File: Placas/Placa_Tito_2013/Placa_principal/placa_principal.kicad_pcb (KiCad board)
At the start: 2 copper layers, 65 x 100 mm, 83 parts, among them IC1 ATMEGA88-P, K1 Servo, K2 Jumper con doble posicion, P1 Puerto Serie, P10 CONN_1, P11 CONN_1, P12 CONN_1, P13 CONN_1, P14 CONN_1, P15 CONN_1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

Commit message: Mejoras a placa principal
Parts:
- removed the 1PIN at (59.5, 65.0)
- removed the 1PIN2mm at (59.5, 65.0)
- removed R1, R2: R sensor, R3
- removed R8, R9: 100, R1
- removed RV5, RV6: POT, PIN_ARRAY_3X1
- removed SERVO_U1, SERVO_U2: CNY70, cny70-4
- added 1PIN: P***, 1pin, F.Cu at (49.5, 63.2)
- added 1PIN: P***, 1pin, F.Cu at (77.5, 63.2)
- added 1PIN: P***, 1pin, F.Cu at (59.5, 63.2)
- U3, U4, U6, U7: moved to B.Cu
- moved RV3 9.46 mm to (85.7, 57.2), turned to 180 degrees
- moved R11 5.09 mm to (82.5, 63.9)
- moved C7 3.96 mm to (42.3, 62.6)
- moved R12 3.58 mm to (45.0, 63.8)
- moved R5 3.08 mm to (30.3, 66.1)
- moved RV2 2.61 mm to (33.1, 64.5)
- moved R6 1.90 mm to (86.4, 64.0)
- moved R7 1.64 mm to (78.2, 78.3)
- moved R10 1.26 mm to (39.8, 66.9)
- moved K2 0.81 mm to (78.7, 127.1)
- moved JP2 0.60 mm to (62.0, 132.0)
- moved P5 0.36 mm to (87.8, 127.2)
- turned U3 to 180 degrees
- turned U4 to 180 degrees
- turned U6 to 180 degrees
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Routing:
- net GND: track 570.2 -> 505.0 mm, vias 6 -> 10
- net /IN_1A: track 149.1 -> 124.3 mm
- net /SENSOR 3: track 134.5 -> 152.9 mm
- net N-000007: track 49.7 -> 38.9 mm, vias 0 -> 1
- net N-0000051: track 9.08 -> 16.5 mm
- net /SCK: track 42.1 -> 36.0 mm
- net /LED3: track 37.9 -> 43.7 mm
- net +8V: track 126.6 -> 132.3 mm, vias 3 -> 2
- net /SENSOR 4: track 88.1 -> 92.5 mm, vias 2 -> 3
- net N-000008: track 6.40 -> 10.6 mm, vias 0 -> 1
- net N-0000050: track 16.3 -> 12.3 mm
- net N-0000054: track 61.5 -> 58.6 mm
- net /IN_2A: track 108.9 -> 106.2 mm
- net /IN_4B: track 30.6 -> 33.3 mm
- net N-0000034: track 5.32 -> 3.02 mm
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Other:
- board size 65 x 100 mm -> 65 x 103.4 mm
- net class Default: via_dia 0.889 -> 1.397

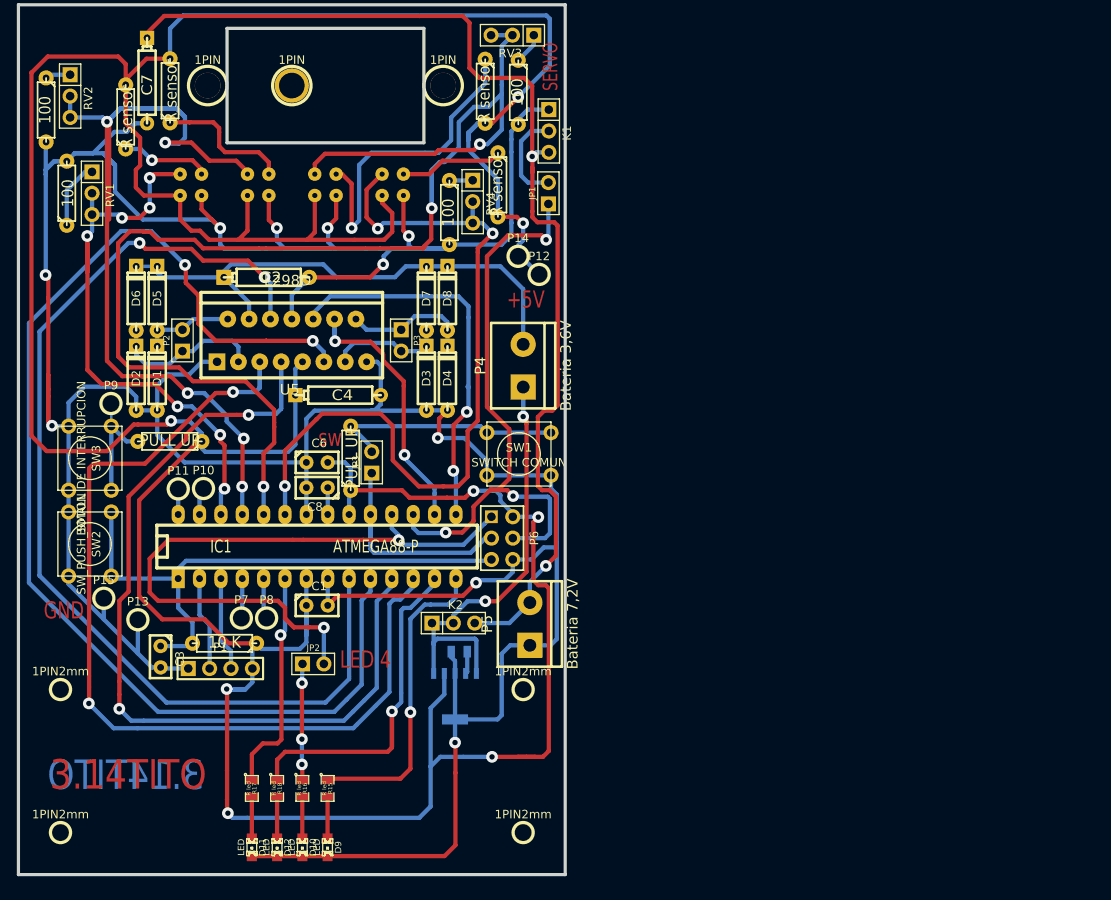
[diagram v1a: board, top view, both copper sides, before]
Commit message: Se termino de routear la placa con los nuevos sensores
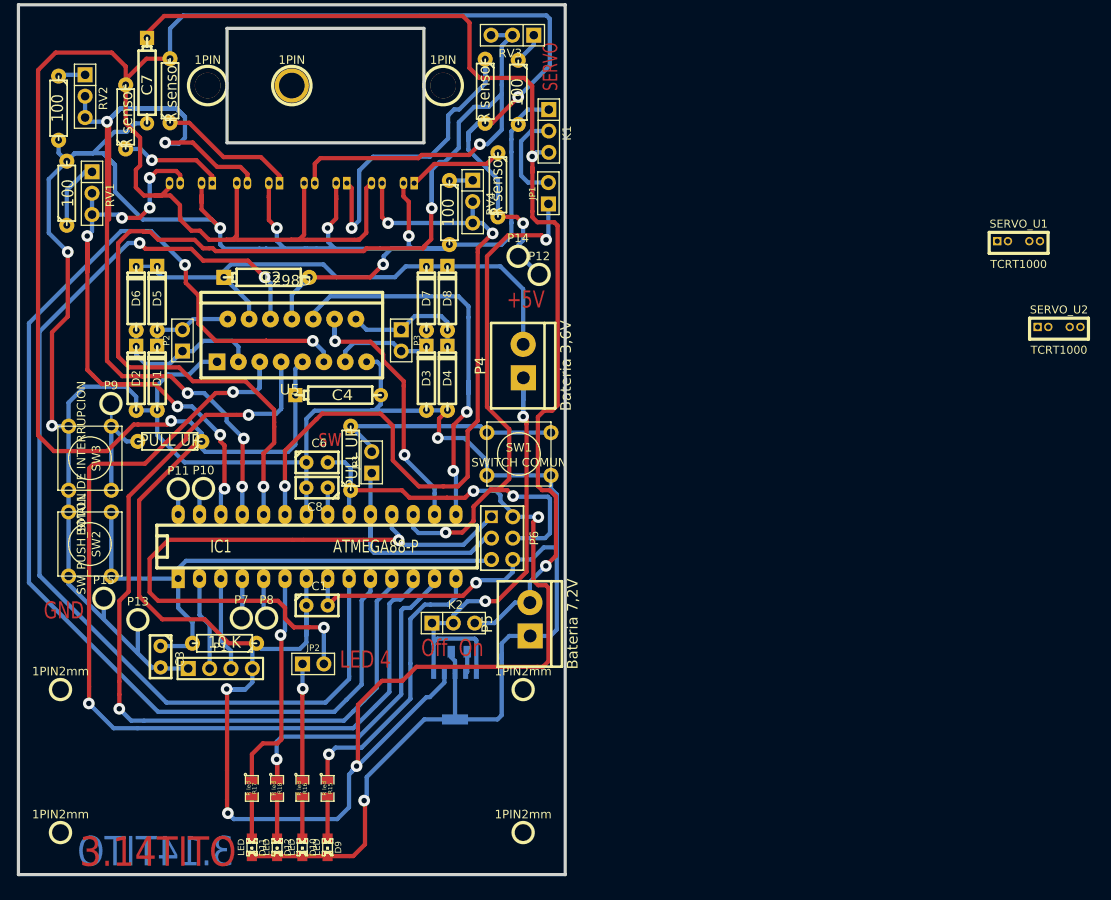
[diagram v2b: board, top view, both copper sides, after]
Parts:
- added SERVO_U1: TCRT1000, TCRT1000, F.Cu at (145.9, 81.9)
- added SERVO_U2: TCRT1000, TCRT1000, F.Cu at (150.7, 92.1)
- U3, U4, U6, U7: value CNY70 -> TCRT1000; footprint cny70-4 -> TCRT1000
- moved RV2 1.78 mm to (34.9, 64.5)
- moved R5 1.50 mm to (31.8, 65.9)
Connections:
- R10 pad 1: N-000008 -> N-0000039
- R11 pad 1: N-000007 -> N-0000037
- R12 pad 1: N-0000051 -> N-0000029
- R13 pad 1: N-0000050 -> N-0000025
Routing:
- net N-0000037: track 0.00 -> 39.4 mm, vias 0 -> 1
- net N-000007: track 38.9 -> 0.00 mm, vias 1 -> 0
- net N-0000029: track 0.00 -> 16.6 mm
- net N-0000051: track 16.5 -> 0.00 mm
- net +5V: track 481.1 -> 494.1 mm
- net N-0000039: track 0.00 -> 12.5 mm, vias 0 -> 1
- net N-0000050: track 12.3 -> 0.00 mm
- net N-0000025: track 0.00 -> 11.5 mm
- net N-000008: track 10.6 -> 0.00 mm, vias 1 -> 0
- net GND: track 505.0 -> 498.3 mm
- net /SENSOR 4: track 92.5 -> 88.3 mm
- net /LED3: track 43.7 -> 40.1 mm
- net /LED1: track 36.9 -> 33.8 mm
- net N-0000040: track 58.6 -> 61.2 mm
- net /SENSOR 3: track 152.9 -> 154.3 mm
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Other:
- board text added: "Off On"

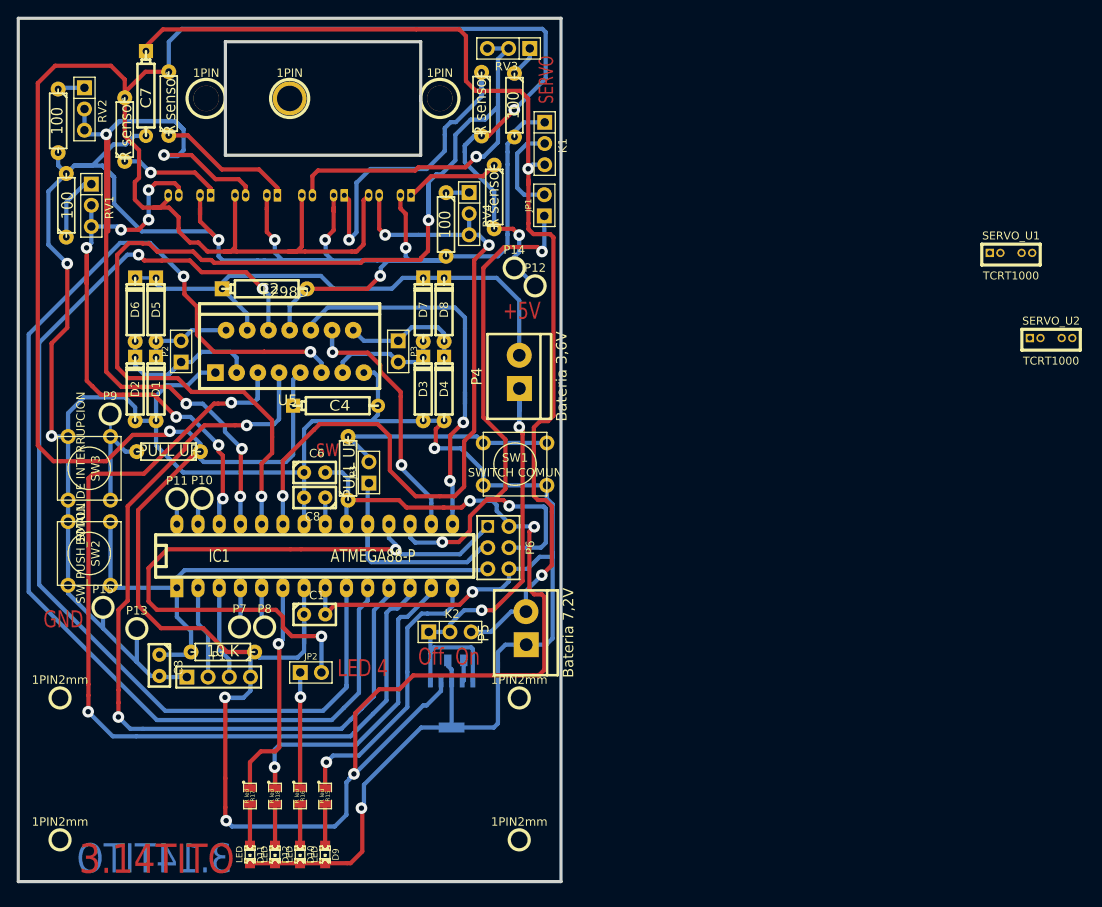
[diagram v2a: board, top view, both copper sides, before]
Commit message: Asociado componente que faltaba, reseteados componentes de la placa.
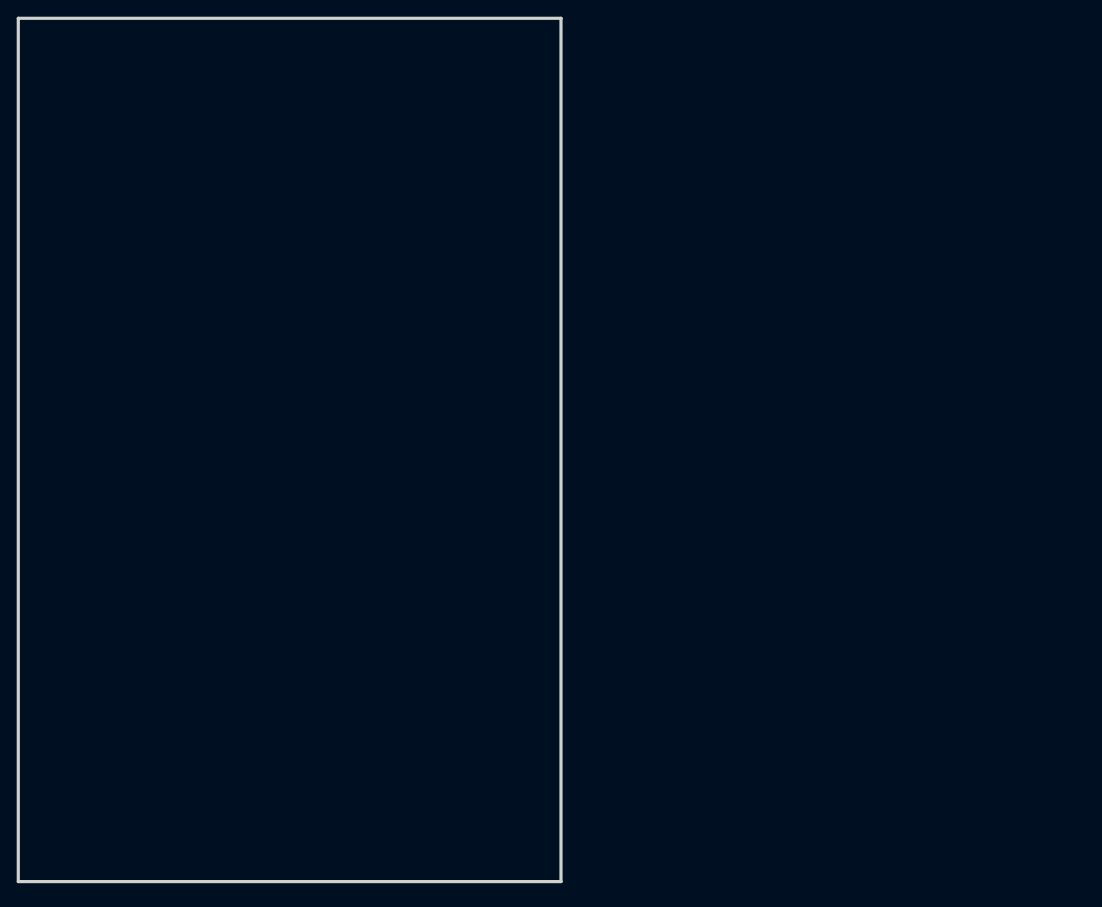
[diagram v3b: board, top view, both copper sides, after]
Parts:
- removed 1PIN (x3): P***, 1pin
- removed 1PIN2mm (x4): P***, 1PIN2mm
- removed C1: 100 nF, C1
- removed C2: 1000 uF, CP4
- removed C3: 100n, C1
- removed C4: 220 uF, CP4
- removed C5: 10 nF, SM0805
- removed C6, C8: 100nF, C1
- removed C7: 100uF, CP4
- removed D1, D2, D3, D4, D5, D6, D7, D8: DIODE, D3
- removed D10, D11, D12, D9: LED, LED-0805
- removed IC1: ATMEGA88-P, DIP-28__300_ELL
- removed JP1, JP2, JP3: JUMPER, PIN_ARRAY_2X1
- removed K1: Servo, PIN_ARRAY_3X1
- removed K2: Jumper con doble posicion, PIN_ARRAY_3X1
- removed P1: Puerto Serie, PIN_ARRAY_4x1
- removed P10, P11, P12, P13, P14, P15, P7, P8, P9: CONN_1, 1PIN2mm
- removed P2: Motor 1, PIN_ARRAY_2X1
- removed P3: Motor 2, PIN_ARRAY_2X1
- removed P4: Bateria 3,6V, bornier2
- removed P5: Bateria 7,2V, bornier2
- removed P6: Programador, pin_array_3x2
- removed R10, R11, R12, R13: R sensor, R3
- removed R14: 10 K, R3
- removed R15, R16, R17, R18: R led, SM0805
- removed R19, R3: PULL UP, R3
- removed R4, R5, R6, R7: 100, R3
- removed RV1, RV2, RV3, RV4: POT, PIN_ARRAY_3X1
- removed SERVO_U1, SERVO_U2, U3, U4, U6, U7: TCRT1000, TCRT1000
- removed SW1: SWITCH COMUN, SW_PUSH_SMALL
- removed SW2: SW_PUSH_SMALL, SW_PUSH_SMALL
- removed SW3: BOTON DE INTERRUPCION, SW_PUSH_SMALL
- removed U5: L298D, L298D
- removed U8: REG_104-5, SOT223-5
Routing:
- net GND: track 498.3 -> 0.00 mm, vias 10 -> 0
- net +5V: track 494.1 -> 0.00 mm, vias 8 -> 0
- net /SENSOR 3: track 154.3 -> 0.00 mm, vias 3 -> 0
- net /ENABLEB: track 141.0 -> 0.00 mm, vias 2 -> 0
- net +8V: track 132.3 -> 0.00 mm, vias 2 -> 0
- net /IN_1A: track 124.3 -> 0.00 mm, vias 2 -> 0
- net /ENABLEA: track 123.2 -> 0.00 mm, vias 2 -> 0
- net /SENSOR 2: track 115.7 -> 0.00 mm, vias 5 -> 0
- net /IN_2A: track 106.2 -> 0.00 mm, vias 2 -> 0
- net /SENSOR 1: track 98.2 -> 0.00 mm, vias 7 -> 0
- net /SENSOR 4: track 88.3 -> 0.00 mm, vias 3 -> 0
- net /LED4: track 83.5 -> 0.00 mm, vias 2 -> 0
- net /MOSI: track 73.4 -> 0.00 mm, vias 3 -> 0
- net /RESET: track 67.4 -> 0.00 mm
- net +BATT: track 63.1 -> 0.00 mm
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- removed copper zone on B.Cu, net (none)
- removed copper zone on F.Cu, net (none)
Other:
- outline, holes or cut-outs redrawn
- board text removed: "+5V"
- board text removed: "3.14TITO"
- board text removed: "GND"
- board text removed: "LED 4"
- board text removed: "Off On"
- board text removed: "SERVO"
- board text removed: "sw"

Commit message: Reempezado el pcb.
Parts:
- added 1PIN2mm: P***, 1PIN2mm, F.Cu at (32.0, 135.0)
- added 1PIN2mm: P***, 1PIN2mm, F.Cu at (32.0, 152.0)
- added 1PIN2mm: P***, 1PIN2mm, F.Cu at (87.0, 152.0)
- added 1PIN2mm: P***, 1PIN2mm, F.Cu at (87.0, 135.0)
- added C1: 100n, SM0805, F.Cu at (157.2, 162.1)
- added C10: 100 n, SM0805, F.Cu at (127.6, 164.0)
- added C11: 100 n, SM0805, F.Cu at (131.3, 164.0)
- added C12: 220 u, C1, F.Cu at (132.9, 143.6)
- added C13: 220 u, C1, F.Cu at (139.4, 145.3)
- added C14: 10 n, SM0805, F.Cu at (116.4, 164.0)
- added C15: 10 n, SM0805, F.Cu at (123.8, 164.0)
- added C2: 15 p, SM0805, F.Cu at (142.4, 164.0)
- added C3: 15 p, SM0805, F.Cu at (149.8, 162.1)
- added C4: 100 n, SM0805, F.Cu at (135.0, 164.0)
- added C5: 10 n, SM0805, F.Cu at (120.1, 162.1)
- added C6: 2200 u, C1, F.Cu at (139.4, 141.6)
- added C7: 10 n, SM0805, F.Cu at (167.4, 159.2)
- added C8: 2,2 u, C1, F.Cu at (145.7, 141.5)
- added C9: 100 u, C1, F.Cu at (124.9, 144.0)
- added D1: LED, LED-0805, F.Cu at (144.4, 179.9)
- added D2: LED, LED-0805, F.Cu at (140.5, 179.9)
- added D3: LED, LED-0805, F.Cu at (136.6, 179.9)
- added D4: LED, LED-0805, F.Cu at (132.7, 179.9)
- added IC1: ATMEGA88A-A, TQFP32, F.Cu at (116.1, 84.8)
- added JP1: PUENTE FALLBACK, PIN_ARRAY_2X1, F.Cu at (183.5, 154.4)
- added JP2: PUENTE FALLBACK, PIN_ARRAY_2X1, F.Cu at (183.5, 159.6)
- added JP3: PUENTE FALLBACK, PIN_ARRAY_2X1, F.Cu at (183.6, 149.9)
- added K1: Servo, PIN_ARRAY_3X1, F.Cu at (162.9, 136.5)
- added P1: ADICIONAL 5V, 1PIN2mm, F.Cu at (121.1, 179.1)
- added P10: Batería 3,6V, bornier2, F.Cu at (147.3, 87.8)
- added P2: ADICIONAL GND, 1PIN2mm, F.Cu at (115.3, 179.1)
- added P3: ADICIONAL 5V, 1PIN2mm, F.Cu at (118.2, 179.1)
- added P4: ADICIONAL GND, 1PIN2mm, F.Cu at (112.4, 179.1)
- added P5: Puerto Serie, PIN_ARRAY_4x1, F.Cu at (182.4, 95.4)
- added P6: Programador, pin_array_3x2, F.Cu at (173.7, 110.6)
- added P7: Motor 1, PIN_ARRAY_2X1, F.Cu at (109.0, 141.1)
- added P8: Motor 2, PIN_ARRAY_2X1, F.Cu at (109.0, 145.2)
- added P9: Batería 7,2V, bornier2, F.Cu at (162.7, 87.9)
- added Q1: BC548, TO92-123, F.Cu at (166.2, 102.6)
- added R1: 220, SM0805, F.Cu at (164.6, 162.1)
- added R10: 180, SM0805, F.Cu at (135.0, 162.1)
- added R11: 180, SM0805, F.Cu at (146.1, 162.1)
- added R12: 180, SM0805, F.Cu at (127.6, 162.1)
- added R13: 180, SM0805, F.Cu at (131.3, 162.1)
- added R14: 180, SM0805, F.Cu at (142.4, 162.1)
- added R15: 100, SM0805, F.Cu at (116.4, 162.1)
- added R16: 100, SM0805, F.Cu at (146.1, 164.0)
- added R17: 100, SM0805, F.Cu at (152.6, 159.2)
- added R18: 100, SM0805, F.Cu at (148.8, 159.2)
- added R19: 100, SM0805, F.Cu at (160.0, 159.2)
- added R2: 220, SM0805, F.Cu at (168.3, 162.1)
- added R20: 100, SM0805, F.Cu at (156.3, 159.2)
- added R3: 220, SM0805, F.Cu at (138.7, 162.1)
- added R4: 220, SM0805, F.Cu at (120.1, 164.0)
- added R5: 10 k, SM0805, F.Cu at (160.9, 162.1)
- added R6: 10 k, SM0805, F.Cu at (153.5, 162.1)
- added R7: 10 K, SM0805, F.Cu at (138.7, 164.0)
- added R8: 47 k, SM0805, F.Cu at (123.8, 162.1)
- added R9: 180, SM0805, F.Cu at (163.7, 159.2)
- added RV1: POT 20 k, PIN_ARRAY_3X1, F.Cu at (163.3, 128.3)
- added RV2: POT 20 k, PIN_ARRAY_3X1, F.Cu at (164.1, 119.8)
- added RV3: POT 20 k, PIN_ARRAY_3X1, F.Cu at (163.8, 124.4)
- added RV4: POT 20 k, PIN_ARRAY_3X1, F.Cu at (162.8, 132.7)
- added RV5: POT 20 k, PIN_ARRAY_3X1, F.Cu at (162.7, 139.4)
- added RV6: POT 20 k, PIN_ARRAY_3X1, F.Cu at (163.5, 144.0)
- added SW1: BOTÓN 1, SW_PUSH_SMALL, F.Cu at (186.9, 121.4)
- added SW2: BOTÓN 2, SW_PUSH_SMALL, F.Cu at (186.9, 109.2)
- added SW3: BOTÓN RESET, SW_PUSH_SMALL, F.Cu at (188.3, 133.7)
- added SW4: INTERRUPTOR BATERÍA 7,2V, MICROSWITCH_SPST, F.Cu at (118.5, 124.0)
- added SW5: INTERRUPTOR BATERÍA 3,7V, MICROSWITCH_SPST, F.Cu at (118.2, 128.5)
- added U1: DRV8833, HTSSOP16, F.Cu at (131.5, 83.5)
- added U2: TCRT1000, TCRT1000, B.Cu at (44.5, 69.5)
- added U3: TCRT1000, TCRT1000, B.Cu at (50.5, 69.5)
- added U4: TCRT1000, TCRT1000, B.Cu at (56.5, 69.5)
- added U5: TCRT1000, TCRT1000, B.Cu at (62.5, 69.5)
- added U6: TCRT1000, TCRT1000, B.Cu at (72.5, 69.5)
- added U7: TCRT1000, TCRT1000, B.Cu at (76.5, 69.5)
- added U8: REG_104-5, SOT223-5, F.Cu at (118.5, 102.4)
- added U9: REG_104-3.3, SOT223-5, F.Cu at (127.9, 102.0)
- added X1: 18,432 M, HC-18UV, F.Cu at (146.8, 101.1)
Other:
- board size 65 x 103.4 mm -> 65 x 104 mm
